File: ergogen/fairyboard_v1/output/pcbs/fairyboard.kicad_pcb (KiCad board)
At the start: 2 copper layers, 305.6 x 118.4 mm, 135 parts

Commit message: feat: mounting for a screen
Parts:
- removed VIK_THROUGHHOLE1: vik-keyboard-throughole, vik-keyboard-throughhole
- added _10: , MountingHole_2.2mm_M2_Pad_Via, F.Cu at (238.1, 143.0)
- added _11: , MountingHole_2.2mm_M2_Pad_Via, F.Cu at (187.4, 124.5)
- added _12: , MountingHole_2.2mm_M2_Pad_Via, F.Cu at (233.5, 124.5)
- added _9: , MountingHole_2.2mm_M2_Pad_Via, F.Cu at (182.8, 143.0)
- moved VIK_OUT1 3.00 mm to (192.5, 149.1)

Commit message: feat: plate mounting holes
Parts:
- added _13: , MountingHole_2.2mm_M2_Pad_Via, F.Cu at (182.8, 143.0)
- added _14: , MountingHole_2.2mm_M2_Pad_Via, F.Cu at (238.1, 143.0)
- added _15: , MountingHole_2.2mm_M2_Pad_Via, F.Cu at (187.4, 124.5)
- added _16: , MountingHole_2.2mm_M2_Pad_Via, F.Cu at (233.5, 124.5)
- _10, _11, _12, _9: footprint MountingHole_2.2mm_M2_Pad_Via -> SpacerHole_3.2mm_M2_Pad_Via
- moved _11 95.6 mm to (94.2, 145.6)
- moved _12 95.6 mm to (326.7, 145.6)
- moved _8 60.2 mm to (272.6, 171.7)
- moved _7 60.2 mm to (148.4, 171.7)
- moved _5 57.2 mm to (121.8, 121.1)
- moved _6 57.2 mm to (299.1, 121.1)
- moved _10 53.7 mm to (255.1, 193.9), turned to 38.75 degrees
- moved _9 53.7 mm to (165.8, 193.9), turned to -38.75 degrees
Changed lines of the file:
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@@
     )
     (module "SpacerHole_3.2mm_M2_Pad_Via" (version 20210722) (generator pcbnew) (layer "F.Cu")
-      (at 148.3585694 171.74267784999998 -14)
+      (at 121.8294928 121.0695035 -14)
       (fp_text reference "_5" (at 0 -3.2) (layer "F.SilkS") hide
         (effects (font (size 1 1) (thickness 0.15)))
@@
     )
     (module "SpacerHole_3.2mm_M2_Pad_Via" (version 20210722) (generator pcbnew) (layer "F.Cu")
-      (at 272.55922519999996 171.74267784999998 14)
+      (at 299.08830179999995 121.0695035 14)
       (fp_text reference "_6" (at 0 -3.2) (layer "F.SilkS") hide
         (effects (font (size 1 1) (thickness 0.15)))
@@
     )
     (module "SpacerHole_3.2mm_M2_Pad_Via" (version 20210722) (generator pcbnew) (layer "F.Cu")
-      (at 94.1716943 145.6073555 -14)
+      (at 148.3585694 171.74267784999998 -14)
       (fp_text reference "_7" (at 0 -3.2) (layer "F.SilkS") hide
         (effects (font (size 1 1) (thickness 0.15)))
@@
     )
     (module "SpacerHole_3.2mm_M2_Pad_Via" (version 20210722) (generator pcbnew) (layer "F.Cu")
+      (at 272.55922519999996 171.74267784999998 14)
+      (fp_text reference "_8" (at 0 -3.2) (layer "F.SilkS") hide
+        (effects (font (size 1 1) (thickness 0.15)))
+      )
+      (fp_circle (center 0 0) (end 2.45 0) (layer "F.CrtYd") (width 0.05) (fill none))
+      (pad "" np_thru_hole circle (at 0 0) (size 3.2 3.2) (drill 3.2) (layers "F&B.Cu" "*.Mask"))
+    )
+    (module "SpacerHole_3.2mm_M2_Pad_Via" (version 20210722) (generator pcbnew) (layer "F.Cu")
+      (at 165.80520504999998 193.92463155 -38.75)
+      (fp_text reference "_9" (at 0 -3.2) (layer "F.SilkS") hide
+        (effects (font (size 1 1) (thickness 0.15)))
+      )
+      (fp_circle (center 0 0) (end 2.45 0) (layer "F.CrtYd") (width 0.05) (fill none))
+      (pad "" np_thru_hole circle (at 0 0) (size 3.2 3.2) (drill 3.2) (layers "F&B.Cu" "*.Mask"))
+    )
+    (module "SpacerHole_3.2mm_M2_Pad_Via" (version 20210722) (generator pcbnew) (layer "F.Cu")
+      (at 255.11258955 193.92463155 38.75)
+      (fp_text reference "_10" (at 0 -3.2) (layer "F.SilkS") hide
+        (effects (font (size 1 1) (thickness 0.15)))
+      )
+      (fp_circle (center 0 0) (end 2.45 0) (layer "F.CrtYd") (width 0.05) (fill none))
+      (pad "" np_thru_hole circle (at 0 0) (size 3.2 3.2) (drill 3.2) (layers "F&B.Cu" "*.Mask"))
+    )
+    (module "SpacerHole_3.2mm_M2_Pad_Via" (version 20210722) (generator pcbnew) (layer "F.Cu")
+      (at 94.1716943 145.6073555 -14)
+      (fp_text reference "_11" (at 0 -3.2) (layer "F.SilkS") hide
+        (effects (font (size 1 1) (thickness 0.15)))
+      )
+      (fp_circle (center 0 0) (end 2.45 0) (layer "F.CrtYd") (width 0.05) (fill none))
+      (pad "" np_thru_hole circle (at 0 0) (size 3.2 3.2) (drill 3.2) (layers "F&B.Cu" "*.Mask"))
+    )
+    (module "SpacerHole_3.2mm_M2_Pad_Via" (version 20210722) (generator pcbnew) (layer "F.Cu")
       (at 326.74610029999997 145.6073555 14)
-      (fp_text reference "_8" (at 0 -3.2) (layer "F.SilkS") hide
+      (fp_text reference "_12" (at 0 -3.2) (layer "F.SilkS") hide
         (effects (font (size 1 1) (thickness 0.15)))
       )
@@
     (module "MountingHole_2.2mm_M2_Pad_Via" (version 20210722) (generator pcbnew) (layer "F.Cu")
       (at 182.8410748 142.980388 -14)
-      (fp_text reference "_9" (at 0 -3.2) (layer "F.SilkS") hide
+      (fp_text reference "_13" (at 0 -3.2) (layer "F.SilkS") hide
         (effects (font (size 1 1) (thickness 0.15)))
       )
@@
     (module "MountingHole_2.2mm_M2_Pad_Via" (version 20210722) (generator pcbnew) (layer "F.Cu")
       (at 238.07671979999998 142.980388 14)
-      (fp_text reference "_10" (at 0 -3.2) (layer "F.SilkS") hide
+      (fp_text reference "_14" (at 0 -3.2) (layer "F.SilkS") hide
         (effects (font (size 1 1) (thickness 0.15)))
       )
@@
     (module "MountingHole_2.2mm_M2_Pad_Via" (version 20210722) (generator pcbnew) (layer "F.Cu")
       (at 187.4375909 124.54476919999999 -14)
-      (fp_text reference "_11" (at 0 -3.2) (layer "F.SilkS") hide
+      (fp_text reference "_15" (at 0 -3.2) (layer "F.SilkS") hide
         (effects (font (size 1 1) (thickness 0.15)))
       )
@@
     (module "MountingHole_2.2mm_M2_Pad_Via" (version 20210722) (generator pcbnew) (layer "F.Cu")
       (at 233.48020369999998 124.54476919999999 14)
-      (fp_text reference "_12" (at 0 -3.2) (layer "F.SilkS") hide
+      (fp_text reference "_16" (at 0 -3.2) (layer "F.SilkS") hide
         (effects (font (size 1 1) (thickness 0.15)))
       )

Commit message: fix: adjust bottom mounting holes
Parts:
- moved _10 86.7 mm to (326.6, 144.8), turned to 14 degrees
- moved _9 86.7 mm to (94.4, 144.8), turned to -14 degrees
- moved _11 86.4 mm to (165.8, 193.9), turned to -38.75 degrees
- moved _12 86.4 mm to (255.1, 193.9), turned to 38.75 degrees
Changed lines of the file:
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@@
     )
     (module "SpacerHole_3.2mm_M2_Pad_Via" (version 20210722) (generator pcbnew) (layer "F.Cu")
-      (at 165.80520504999998 193.92463155 -38.75)
+      (at 94.3652318 144.8311189 -14)
       (fp_text reference "_9" (at 0 -3.2) (layer "F.SilkS") hide
         (effects (font (size 1 1) (thickness 0.15)))
@@
     )
     (module "SpacerHole_3.2mm_M2_Pad_Via" (version 20210722) (generator pcbnew) (layer "F.Cu")
-      (at 255.11258955 193.92463155 38.75)
+      (at 326.5525628 144.8311189 14)
       (fp_text reference "_10" (at 0 -3.2) (layer "F.SilkS") hide
         (effects (font (size 1 1) (thickness 0.15)))
@@
     )
     (module "SpacerHole_3.2mm_M2_Pad_Via" (version 20210722) (generator pcbnew) (layer "F.Cu")
-      (at 94.1716943 145.6073555 -14)
+      (at 165.80520504999998 193.92463155 -38.75)
       (fp_text reference "_11" (at 0 -3.2) (layer "F.SilkS") hide
         (effects (font (size 1 1) (thickness 0.15)))
@@
     )
     (module "SpacerHole_3.2mm_M2_Pad_Via" (version 20210722) (generator pcbnew) (layer "F.Cu")
-      (at 326.74610029999997 145.6073555 14)
+      (at 255.11258955 193.92463155 38.75)
       (fp_text reference "_12" (at 0 -3.2) (layer "F.SilkS") hide
         (effects (font (size 1 1) (thickness 0.15)))

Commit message: feat: increase fillet size to prevent DRC error
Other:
- board size 305.6 x 118.4 mm -> 305.6 x 118.3 mm

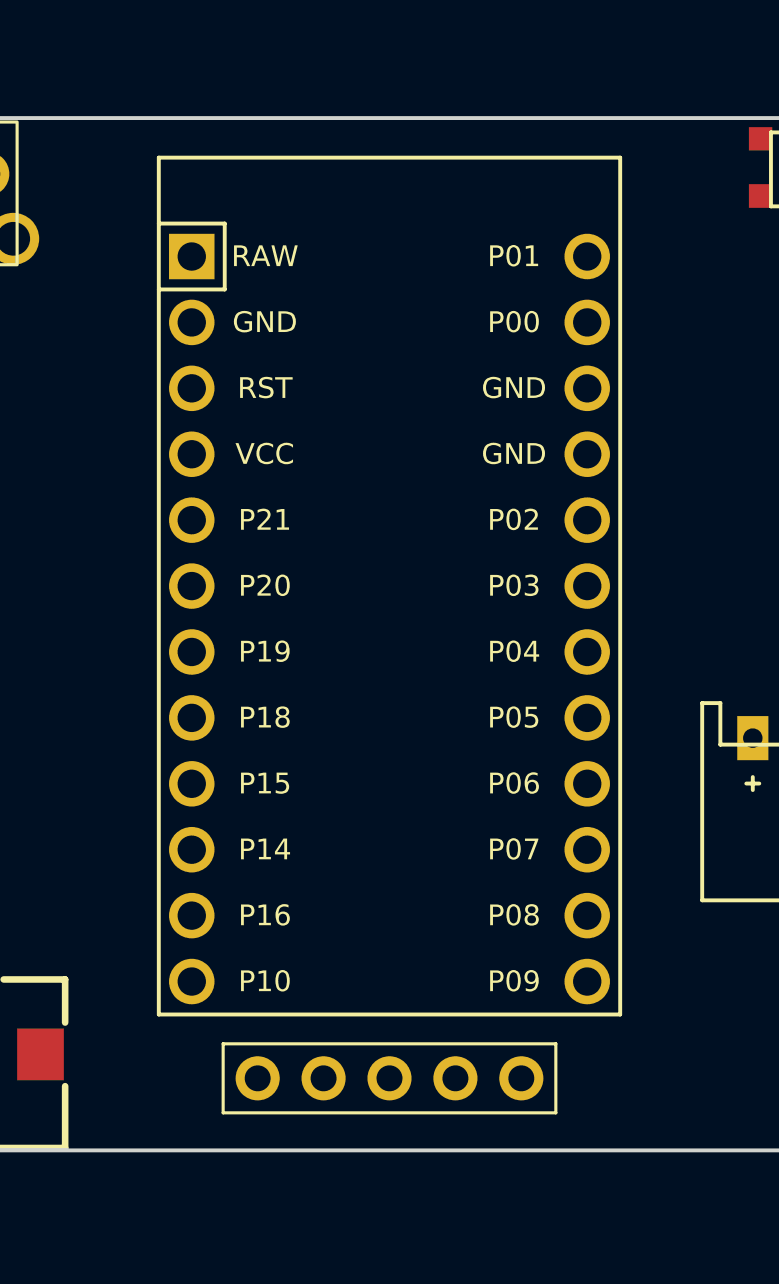
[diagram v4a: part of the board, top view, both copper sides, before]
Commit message: feat: added nice_nano and elite_c compatible footprint
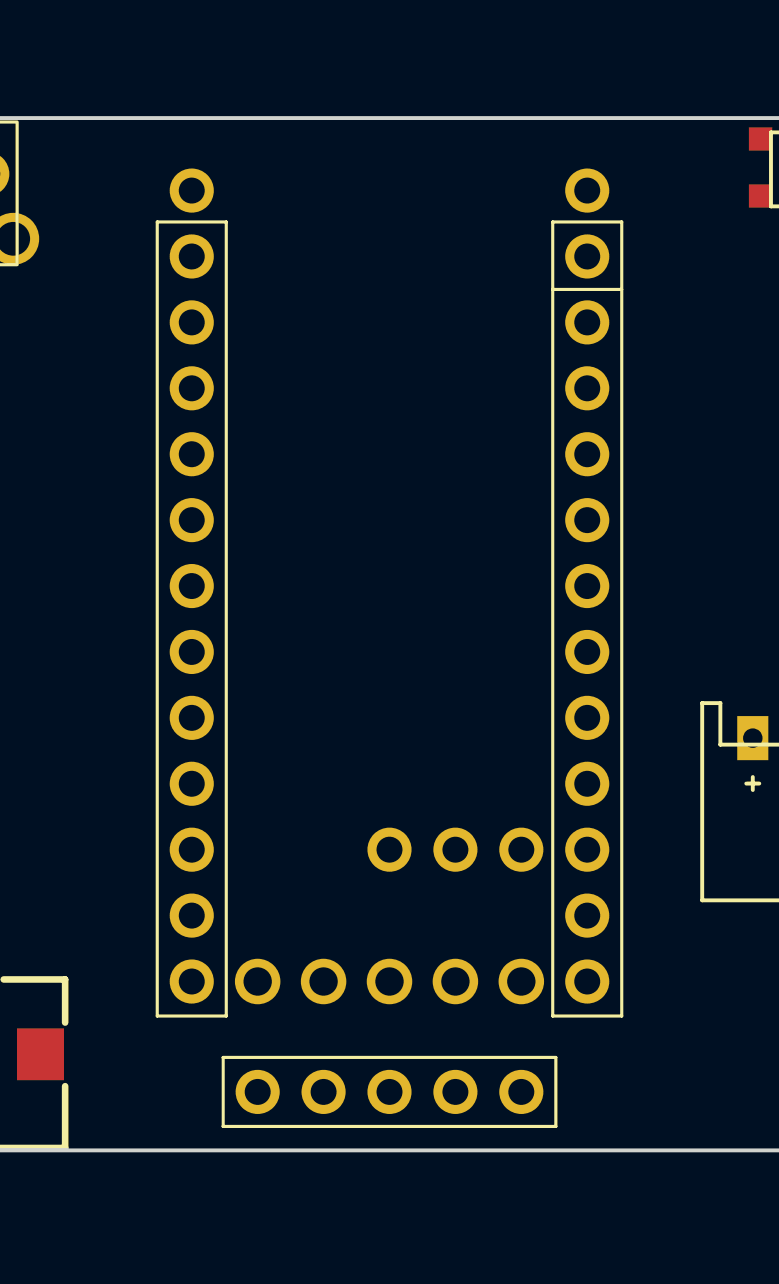
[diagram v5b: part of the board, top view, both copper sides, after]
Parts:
- removed MCU1: , ProMicro
- removed _1: , SpacerHole_3.2mm_M2_Pad_Via
- added ?: , nice_nano_elite_c, F.Cu at (210.5, 131.8)
- added _17: , MountingHole_2.2mm_M2_Pad_Via, F.Cu at (233.5, 124.5)
- _13: footprint MountingHole_2.2mm_M2_Pad_Via -> SpacerHole_3.2mm_M2_Pad_Via
- moved _4 257.0 mm to (81.9, 124.0), turned to -14 degrees
- moved _10 232.2 mm to (94.4, 144.8), turned to -14 degrees
- moved _5 217.2 mm to (339.0, 124.0), turned to 14 degrees
- moved _3 181.8 mm to (263.4, 134.9), turned to 14 degrees
- moved _9 180.2 mm to (272.6, 171.7), turned to 14 degrees
- moved _6 177.3 mm to (121.8, 121.1), turned to -14 degrees
- moved _11 168.1 mm to (326.6, 144.8), turned to 14 degrees
- moved _7 159.0 mm to (299.1, 121.1), turned to 14 degrees
- moved _8 124.2 mm to (148.4, 171.7), turned to -14 degrees
- moved _2 105.8 mm to (157.6, 134.9), turned to -14 degrees
- moved _12 89.3 mm to (165.8, 193.9), turned to -38.75 degrees
- moved _13 88.4 mm to (255.1, 193.9), turned to 38.75 degrees
- moved _14 55.2 mm to (182.8, 143.0), turned to -14 degrees
- moved _15 53.9 mm to (238.1, 143.0), turned to 14 degrees
- moved _16 46.0 mm to (187.4, 124.5), turned to -14 degrees
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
